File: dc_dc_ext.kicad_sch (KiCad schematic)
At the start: 30 parts

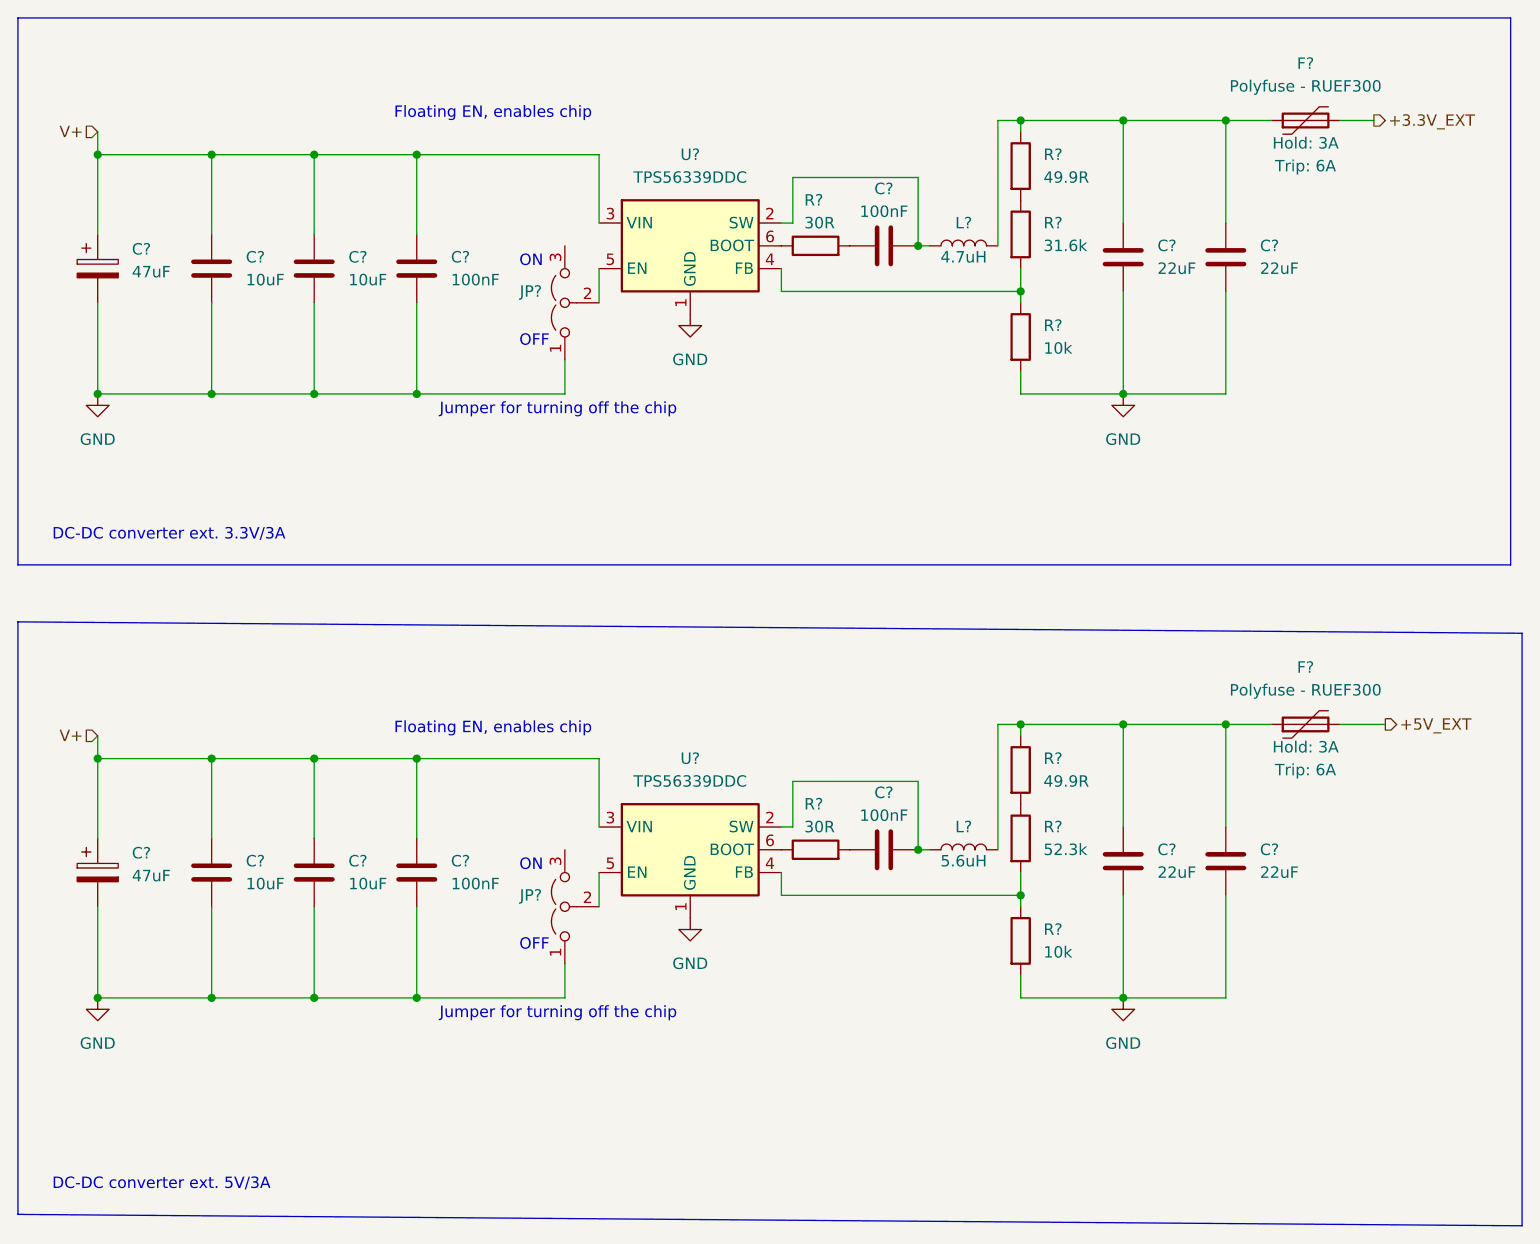
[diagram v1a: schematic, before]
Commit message: annotated all schematics, modified ext_devices
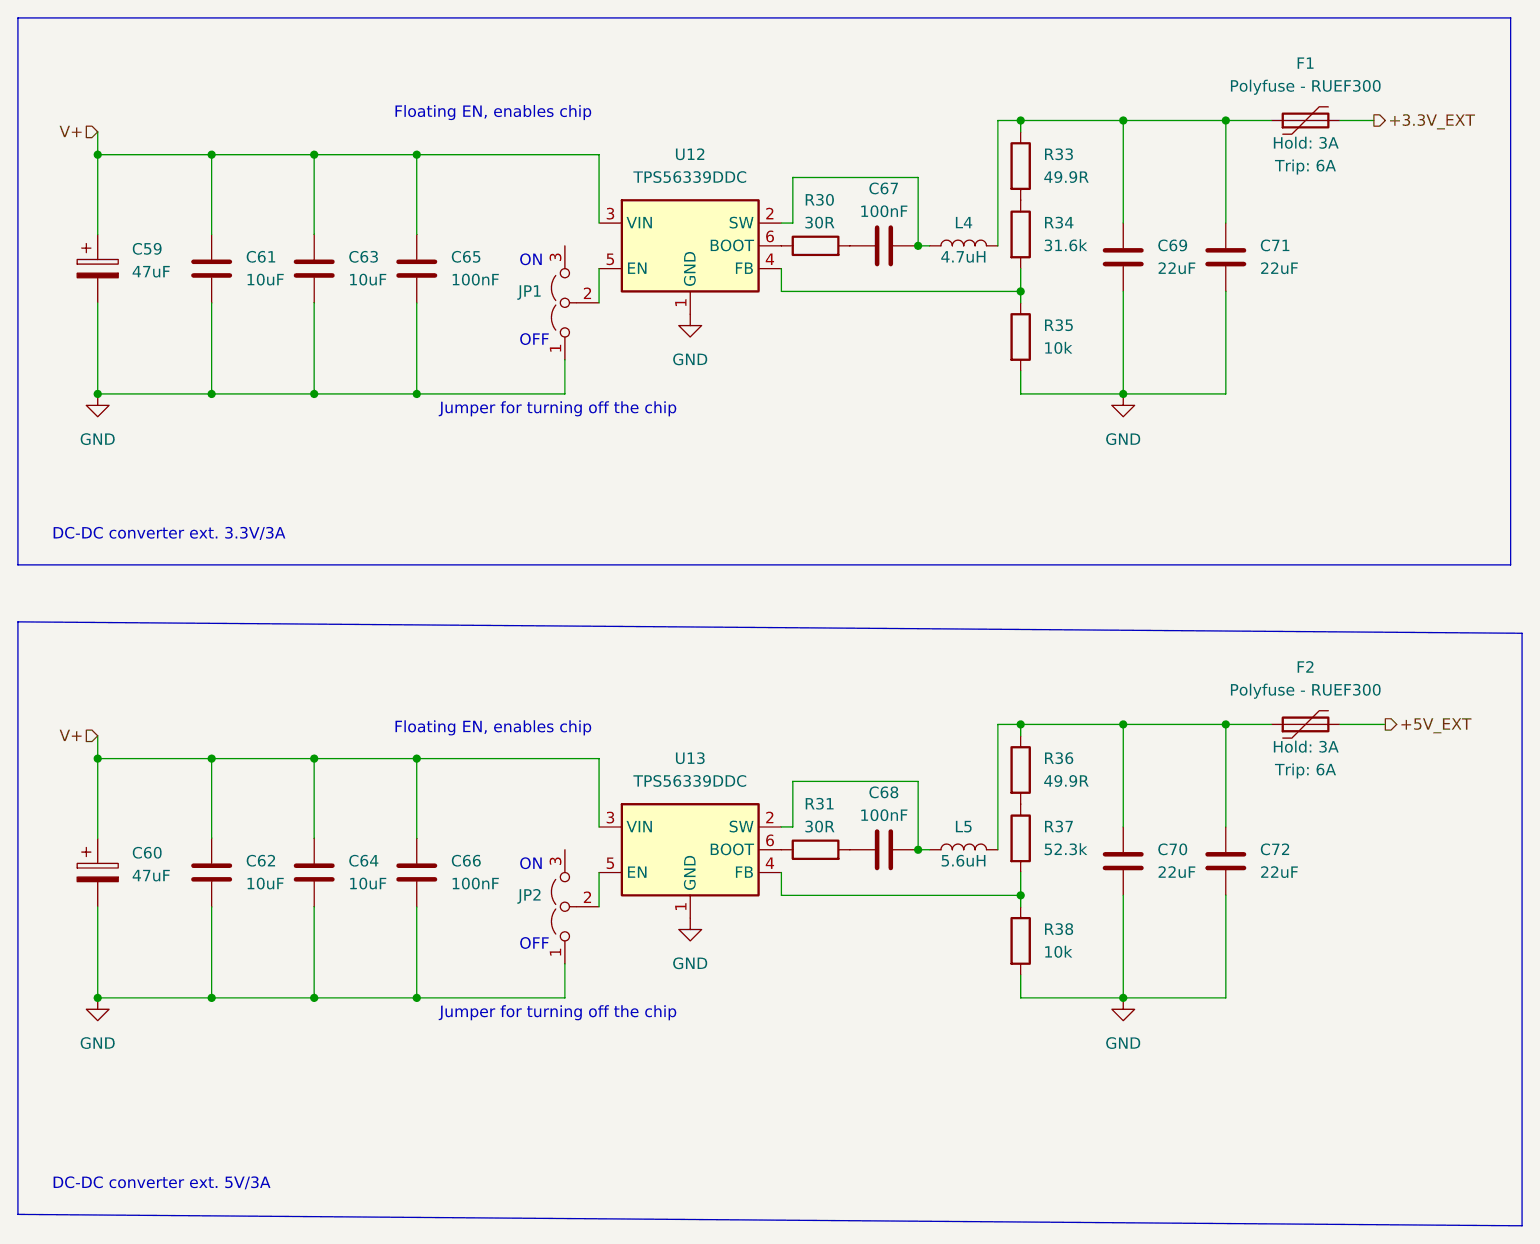
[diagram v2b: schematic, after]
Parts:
- gave numbers to parts that had none: 30
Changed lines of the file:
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@@
   (symbol (lib_id "Device:L") (at 167.64 118.745 90) (unit 1)
     (in_bom yes) (on_board yes)
-    (property "Reference" "L?" (id 0) (at 167.64 116.205 90))
+    (property "Reference" "L5" (id 0) (at 167.64 116.205 90))
     (property "Value" "5.6uH" (id 1) (at 167.64 120.015 90))
     (property "Footprint" "Robotont:IND-JSHC0650-5R6M" (id 2) (at 167.64 118.745 0)
@@
   (symbol (lib_id "Device:R") (at 173.99 42.545 0) (unit 1)
     (in_bom yes) (on_board yes)
-    (property "Reference" "R?" (id 0) (at 176.53 41.2749 0)
+    (property "Reference" "R33" (id 0) (at 176.53 41.2749 0)
       (effects (font (size 1.27 1.27)) (justify left))
     )
@@
   (symbol (lib_id "Device:C") (at 185.42 52.705 0) (unit 1)
     (in_bom yes) (on_board yes) (fields_autoplaced)
-    (property "Reference" "C?" (id 0) (at 189.23 51.4349 0)
+    (property "Reference" "C69" (id 0) (at 189.23 51.4349 0)
       (effects (font (size 1.27 1.27)) (justify left))
     )
@@
   (symbol (lib_id "Regulator_Switching:TPS56339DDC") (at 137.16 118.745 0) (unit 1)
     (in_bom yes) (on_board yes) (fields_autoplaced)
-    (property "Reference" "U?" (id 0) (at 137.16 108.585 0))
+    (property "Reference" "U13" (id 0) (at 137.16 108.585 0))
     (property "Value" "TPS56339DDC" (id 1) (at 137.16 111.125 0))
     (property "Footprint" "Package_TO_SOT_SMD:TSOT-23-6" (id 2) (at 138.43 125.095 0)
@@
   (symbol (lib_id "Device:C") (at 106.68 121.285 0) (unit 1)
     (in_bom yes) (on_board yes) (fields_autoplaced)
-    (property "Reference" "C?" (id 0) (at 110.49 120.0149 0)
+    (property "Reference" "C66" (id 0) (at 110.49 120.0149 0)
       (effects (font (size 1.27 1.27)) (justify left))
     )
@@
   (symbol (lib_id "Device:R") (at 173.99 128.905 0) (unit 1)
     (in_bom yes) (on_board yes)
-    (property "Reference" "R?" (id 0) (at 176.53 127.6349 0)
+    (property "Reference" "R38" (id 0) (at 176.53 127.6349 0)
       (effects (font (size 1.27 1.27)) (justify left))
     )
@@
   (symbol (lib_id "Device:C_Polarized") (at 71.12 121.285 0) (unit 1)
     (in_bom yes) (on_board yes) (fields_autoplaced)
-    (property "Reference" "C?" (id 0) (at 74.93 119.1259 0)
+    (property "Reference" "C60" (id 0) (at 74.93 119.1259 0)
       (effects (font (size 1.27 1.27)) (justify left))
     )
@@
   (symbol (lib_id "Jumper:Jumper_3_Open") (at 123.19 125.095 90) (unit 1)
     (in_bom yes) (on_board yes) (fields_autoplaced)
-    (property "Reference" "JP?" (id 0) (at 120.65 123.8249 90)
+    (property "Reference" "JP2" (id 0) (at 120.65 123.8249 90)
       (effects (font (size 1.27 1.27)) (justify left))
     )
@@
   (symbol (lib_id "Device:C") (at 95.25 53.975 0) (unit 1)
     (in_bom yes) (on_board yes) (fields_autoplaced)
-    (property "Reference" "C?" (id 0) (at 99.06 52.7049 0)
+    (property "Reference" "C63" (id 0) (at 99.06 52.7049 0)
       (effects (font (size 1.27 1.27)) (justify left))
     )
@@
   (symbol (lib_id "Device:R") (at 173.99 117.475 0) (unit 1)
     (in_bom yes) (on_board yes)
-    (property "Reference" "R?" (id 0) (at 176.53 116.2049 0)
+    (property "Reference" "R37" (id 0) (at 176.53 116.2049 0)
       (effects (font (size 1.27 1.27)) (justify left))
     )
@@
   (symbol (lib_id "Device:C") (at 196.85 52.705 0) (unit 1)
     (in_bom yes) (on_board yes) (fields_autoplaced)
-    (property "Reference" "C?" (id 0) (at 200.66 51.4349 0)
+    (property "Reference" "C71" (id 0) (at 200.66 51.4349 0)
       (effects (font (size 1.27 1.27)) (justify left))
     )
@@
   (symbol (lib_id "Device:R") (at 151.13 51.435 90) (unit 1)
     (in_bom yes) (on_board yes)
-    (property "Reference" "R?" (id 0) (at 149.86 46.355 90)
+    (property "Reference" "R30" (id 0) (at 149.86 46.355 90)
       (effects (font (size 1.27 1.27)) (justify right))
     )
@@
   (symbol (lib_id "Regulator_Switching:TPS56339DDC") (at 137.16 51.435 0) (unit 1)
     (in_bom yes) (on_board yes) (fields_autoplaced)
-    (property "Reference" "U?" (id 0) (at 137.16 41.275 0))
+    (property "Reference" "U12" (id 0) (at 137.16 41.275 0))
     (property "Value" "TPS56339DDC" (id 1) (at 137.16 43.815 0))
     (property "Footprint" "Package_TO_SOT_SMD:TSOT-23-6" (id 2) (at 138.43 57.785 0)
@@
   (symbol (lib_id "Device:C") (at 158.75 51.435 90) (unit 1)
     (in_bom yes) (on_board yes)
-    (property "Reference" "C?" (id 0) (at 158.75 45.085 90))
+    (property "Reference" "C67" (id 0) (at 158.75 45.085 90))
     (property "Value" "100nF" (id 1) (at 158.75 47.625 90))
     (property "Footprint" "Capacitor_SMD:C_0805_2012Metric_Pad1.18x1.45mm_HandSolder" (id 2) (at 162.56 50.4698 0)
@@
   (symbol (lib_id "Device:R") (at 151.13 118.745 90) (unit 1)
     (in_bom yes) (on_board yes)
-    (property "Reference" "R?" (id 0) (at 149.86 113.665 90)
+    (property "Reference" "R31" (id 0) (at 149.86 113.665 90)
       (effects (font (size 1.27 1.27)) (justify right))
     )
@@
   (symbol (lib_id "Device:R") (at 173.99 50.165 0) (unit 1)
     (in_bom yes) (on_board yes)
-    (property "Reference" "R?" (id 0) (at 176.53 48.8949 0)
+    (property "Reference" "R34" (id 0) (at 176.53 48.8949 0)
       (effects (font (size 1.27 1.27)) (justify left))
     )
@@
   (symbol (lib_id "Device:Polyfuse") (at 205.74 37.465 90) (unit 1)
     (in_bom yes) (on_board yes)
-    (property "Reference" "F?" (id 0) (at 205.74 31.115 90))
+    (property "Reference" "F1" (id 0) (at 205.74 31.115 90))
     (property "Value" "Polyfuse  - RUEF300" (id 1) (at 205.74 33.655 90))
     (property "Footprint" "Robotont:FUSE-RUEF300" (id 2) (at 210.82 36.195 0)
@@
   (symbol (lib_id "Device:C") (at 83.82 121.285 0) (unit 1)
     (in_bom yes) (on_board yes) (fields_autoplaced)
-    (property "Reference" "C?" (id 0) (at 87.63 120.0149 0)
+    (property "Reference" "C62" (id 0) (at 87.63 120.0149 0)
       (effects (font (size 1.27 1.27)) (justify left))
     )
@@
   (symbol (lib_id "Device:R") (at 173.99 61.595 0) (unit 1)
     (in_bom yes) (on_board yes)
-    (property "Reference" "R?" (id 0) (at 176.53 60.3249 0)
+    (property "Reference" "R35" (id 0) (at 176.53 60.3249 0)
       (effects (font (size 1.27 1.27)) (justify left))
     )
@@
   (symbol (lib_id "Device:R") (at 173.99 109.855 0) (unit 1)
     (in_bom yes) (on_board yes)
-    (property "Reference" "R?" (id 0) (at 176.53 108.5849 0)
+    (property "Reference" "R36" (id 0) (at 176.53 108.5849 0)
       (effects (font (size 1.27 1.27)) (justify left))
     )
@@
   (symbol (lib_id "Device:Polyfuse") (at 205.74 104.775 90) (unit 1)
     (in_bom yes) (on_board yes)
-    (property "Reference" "F?" (id 0) (at 205.74 98.425 90))
+    (property "Reference" "F2" (id 0) (at 205.74 98.425 90))
     (property "Value" "Polyfuse  - RUEF300" (id 1) (at 205.74 100.965 90))
     (property "Footprint" "Robotont:FUSE-RUEF300" (id 2) (at 210.82 103.505 0)
@@
   (symbol (lib_id "Device:C") (at 158.75 118.745 90) (unit 1)
     (in_bom yes) (on_board yes)
-    (property "Reference" "C?" (id 0) (at 158.75 112.395 90))
+    (property "Reference" "C68" (id 0) (at 158.75 112.395 90))
     (property "Value" "100nF" (id 1) (at 158.75 114.935 90))
     (property "Footprint" "Capacitor_SMD:C_0805_2012Metric_Pad1.18x1.45mm_HandSolder" (id 2) (at 162.56 117.7798 0)
@@
   (symbol (lib_id "Device:C") (at 196.85 120.015 0) (unit 1)
     (in_bom yes) (on_board yes) (fields_autoplaced)
-    (property "Reference" "C?" (id 0) (at 200.66 118.7449 0)
+    (property "Reference" "C72" (id 0) (at 200.66 118.7449 0)
       (effects (font (size 1.27 1.27)) (justify left))
     )
@@
   (symbol (lib_id "Device:L") (at 167.64 51.435 90) (unit 1)
     (in_bom yes) (on_board yes)
-    (property "Reference" "L?" (id 0) (at 167.64 48.895 90))
+    (property "Reference" "L4" (id 0) (at 167.64 48.895 90))
     (property "Value" "4.7uH" (id 1) (at 167.64 52.705 90))
     (property "Footprint" "Robotont:IND-FXL1040-4R7-M" (id 2) (at 167.64 51.435 0)
@@
   (symbol (lib_id "Device:C") (at 185.42 120.015 0) (unit 1)
     (in_bom yes) (on_board yes) (fields_autoplaced)
-    (property "Reference" "C?" (id 0) (at 189.23 118.7449 0)
+    (property "Reference" "C70" (id 0) (at 189.23 118.7449 0)
       (effects (font (size 1.27 1.27)) (justify left))
     )
@@
   (symbol (lib_id "Device:C") (at 95.25 121.285 0) (unit 1)
     (in_bom yes) (on_board yes) (fields_autoplaced)
-    (property "Reference" "C?" (id 0) (at 99.06 120.0149 0)
+    (property "Reference" "C64" (id 0) (at 99.06 120.0149 0)
       (effects (font (size 1.27 1.27)) (justify left))
     )
@@
   (symbol (lib_id "Device:C_Polarized") (at 71.12 53.975 0) (unit 1)
     (in_bom yes) (on_board yes) (fields_autoplaced)
-    (property "Reference" "C?" (id 0) (at 74.93 51.8159 0)
+    (property "Reference" "C59" (id 0) (at 74.93 51.8159 0)
       (effects (font (size 1.27 1.27)) (justify left))
     )
@@
   (symbol (lib_id "Device:C") (at 106.68 53.975 0) (unit 1)
     (in_bom yes) (on_board yes) (fields_autoplaced)
-    (property "Reference" "C?" (id 0) (at 110.49 52.7049 0)
+    (property "Reference" "C65" (id 0) (at 110.49 52.7049 0)
       (effects (font (size 1.27 1.27)) (justify left))
     )
@@
   (symbol (lib_id "Device:C") (at 83.82 53.975 0) (unit 1)
     (in_bom yes) (on_board yes) (fields_autoplaced)
-    (property "Reference" "C?" (id 0) (at 87.63 52.7049 0)
+    (property "Reference" "C61" (id 0) (at 87.63 52.7049 0)
       (effects (font (size 1.27 1.27)) (justify left))
     )
@@
   (symbol (lib_id "Jumper:Jumper_3_Open") (at 123.19 57.785 90) (unit 1)
     (in_bom yes) (on_board yes) (fields_autoplaced)
-    (property "Reference" "JP?" (id 0) (at 120.65 56.5149 90)
-      (effects (font (size 1.27 1.27)) (justify left))
-    )
+    (property "Reference" "JP1" (id 0) (at 120.65 56.5149 90)
+      (effects (font (size 1.27 1.27)) (justify left))
+    )

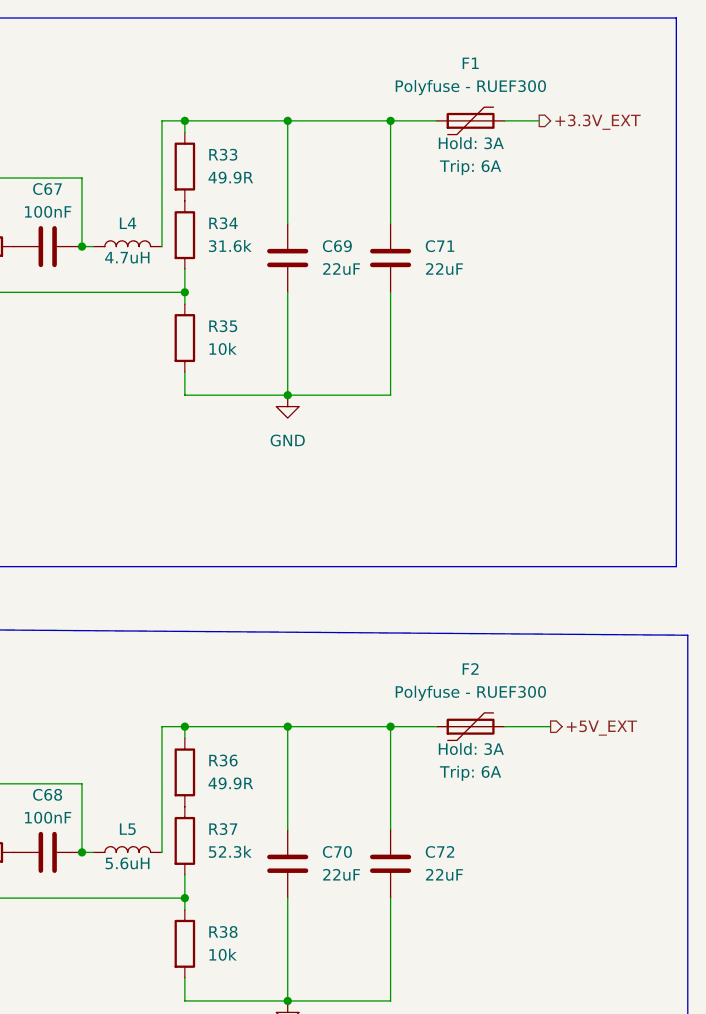
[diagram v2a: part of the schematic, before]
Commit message: changed ext power fuses
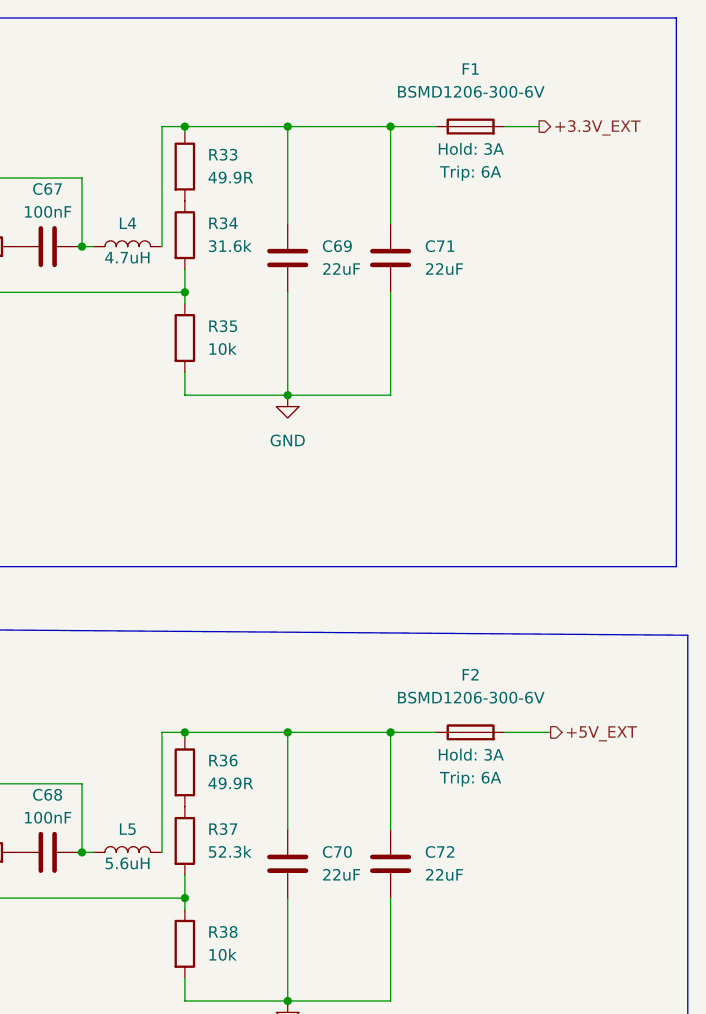
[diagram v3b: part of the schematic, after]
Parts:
- removed F1, F2: Polyfuse - RUEF300, Robotont:FUSE-RUEF300, symbol Device:Polyfuse
- added F1, F2: BSMD1206-300-6V, Fuse:Fuse_1206_3216Metric_Pad1.42x1.75mm_HandSolder, symbol Device:Fuse
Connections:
- net +3.3V_EXT: now also F1.2
- net +5V_EXT: now also F2.2
- net at C70.1, C72.1, L5.2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: now also F2.1
- net at C69.1, C71.1, L4.2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: now also F1.1
